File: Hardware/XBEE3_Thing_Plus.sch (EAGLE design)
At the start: 43 parts, among them Q1 2.5A/30V, U1 XBEE3_Micro, U2 MCP73831, U3 AP2112K-3.3V, U4 CP2102N

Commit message: v01 update
Removed test points from bottom of the board, removed the trace antenna, and modified the top ground pour as outlined in the XBee3 datasheet
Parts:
- removed E1: ANTENNA-GROUNDEDTRACE-15.2M_FLIPPED, SparkFun-RF:ANTENNA-GROUNDEDTRACE-15.2M_FLIPPED
- removed JP1: JUMPER-SMT_2_NC_TRACE_NO-SILK, SparkFun-Jumpers:JUMPER-SMT_2_NC_TRACE_NO-SILK
- added H1, H2: STAND-OFF, SparkFun-Hardware:STAND-OFF
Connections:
- removed net N$1: E1.SIGNAL, JP1.2
- removed net RF: JP1.1, U1.RF
- net GND: no longer E1.GND
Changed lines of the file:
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@@
 <part name="H3" library="SparkFun-Hardware" deviceset="STAND-OFF" device=""/>
 <part name="H4" library="SparkFun-Hardware" deviceset="STAND-OFF" device=""/>
-<part name="JP1" library="SparkFun-Jumpers" deviceset="JUMPER-SMT_2_NC_TRACE" device="_NO-SILK" value=""/>
 <part name="GND26" library="SparkFun-Aesthetics" deviceset="GND" device=""/>
 <part name="SUPPLY14" library="SparkFun-Aesthetics" deviceset="V_USB" device=""/>
@@
 <part name="FD3" library="SparkFun-Aesthetics" deviceset="FIDUCIAL" device="UFIDUCIAL" value="FIDUCIALUFIDUCIAL"/>
 <part name="FD4" library="SparkFun-Aesthetics" deviceset="FIDUCIAL" device="UFIDUCIAL" value="FIDUCIALUFIDUCIAL"/>
-<part name="E1" library="SparkFun-RF" deviceset="ANTENNA-GROUNDED" device="TRACE-15.2M_FLIPPED"/>
-<part name="GND18" library="SparkFun-PowerSymbols" deviceset="GND" device=""/>
 <part name="U$63" library="SparkFun-Aesthetics" deviceset="QWIIC_LOGO" device="_5MM" value="QWIIC_LOGO_5MM"/>
 <part name="J4" library="SparkFun-Connectors" deviceset="JST_2MM_MALE" device=""/>
 <part name="LOGO1" library="SparkFun-Aesthetics" deviceset="SFE_LOGO_NAME_FLAME" device=".1_INCH" value="SFE_LOGO_NAME_FLAME.1_INCH"/>
 <part name="LOGO2" library="SparkFun-Aesthetics" deviceset="OSHW-LOGO" device="S" value="OSHW-LOGOS"/>
+<part name="H1" library="SparkFun-Hardware" deviceset="STAND-OFF" device=""/>
+<part name="H2" library="SparkFun-Hardware" deviceset="STAND-OFF" device=""/>
 </parts>
 <sheets>
@@
 <instance part="H3" gate="G$1" x="241.3" y="33.02" smashed="yes"/>
 <instance part="H4" gate="G$1" x="241.3" y="30.48" smashed="yes"/>
-<instance part="JP1" gate="G$1" x="167.64" y="83.82" smashed="yes">
-<attribute name="NAME" x="165.1" y="86.36" size="1.778" layer="95" font="vector"/>
-<attribute name="VALUE" x="165.1" y="81.28" size="1.778" layer="96" font="vector" align="top-left"/>
-</instance>
 <instance part="GND26" gate="1" x="15.24" y="58.42" smashed="yes">
 <attribute name="VALUE" x="12.7" y="55.88" size="1.778" layer="96"/>
@@
 <instance part="FD3" gate="G$1" x="233.68" y="33.02" smashed="yes"/>
 <instance part="FD4" gate="G$1" x="233.68" y="30.48" smashed="yes"/>
-<instance part="E1" gate="G$1" x="175.26" y="96.52" smashed="yes">
-<attribute name="NAME" x="178.308" y="91.44" size="1.778" layer="95" font="vector"/>
-</instance>
-<instance part="GND18" gate="1" x="177.8" y="78.74" smashed="yes">
-<attribute name="VALUE" x="177.8" y="78.486" size="1.778" layer="96" align="top-center"/>
-</instance>
 <instance part="U$63" gate="G$1" x="137.16" y="5.08" smashed="yes"/>
 <instance part="J4" gate="G$1" x="167.64" y="160.02" smashed="yes" rot="MR90">
@@
 <instance part="LOGO1" gate="G$1" x="190.5" y="35.56" smashed="yes"/>
 <instance part="LOGO2" gate="G$1" x="113.538" y="11.176" smashed="yes"/>
+<instance part="H1" gate="G$1" x="243.84" y="30.48" smashed="yes"/>
+<instance part="H2" gate="G$1" x="243.84" y="33.02" smashed="yes"/>
 </instances>
 <busses>
@@
 <wire x1="228.6" y1="154.94" x2="233.68" y2="154.94" width="0.1524" layer="91"/>
 <label x="233.68" y="154.94" size="1.27" layer="95" rot="MR180" xref="yes"/>
-</segment>
-</net>
-<net name="RF" class="0">
-<segment>
-<pinref part="U1" gate="G$1" pin="RF"/>
-<pinref part="JP1" gate="G$1" pin="1"/>
-<wire x1="157.48" y1="83.82" x2="162.56" y2="83.82" width="0.1524" layer="91"/>
 </segment>
 </net>
@@
 <pinref part="GND17" gate="1" pin="GND"/>
 <wire x1="22.86" y1="15.24" x2="22.86" y2="12.7" width="0.1524" layer="91"/>
-</segment>
-<segment>
-<pinref part="E1" gate="G$1" pin="GND"/>
-<wire x1="177.8" y1="86.36" x2="177.8" y2="81.28" width="0.1524" layer="91"/>
-<pinref part="GND18" gate="1" pin="GND"/>
 </segment>
 <segment>
@@
 </segment>
 </net>
-<net name="N$1" class="0">
-<segment>
-<pinref part="JP1" gate="G$1" pin="2"/>
-<wire x1="175.26" y1="86.36" x2="175.26" y2="83.82" width="0.1524" layer="91"/>
-<wire x1="175.26" y1="83.82" x2="172.72" y2="83.82" width="0.1524" layer="91"/>
-<pinref part="E1" gate="G$1" pin="SIGNAL"/>
-</segment>
-</net>

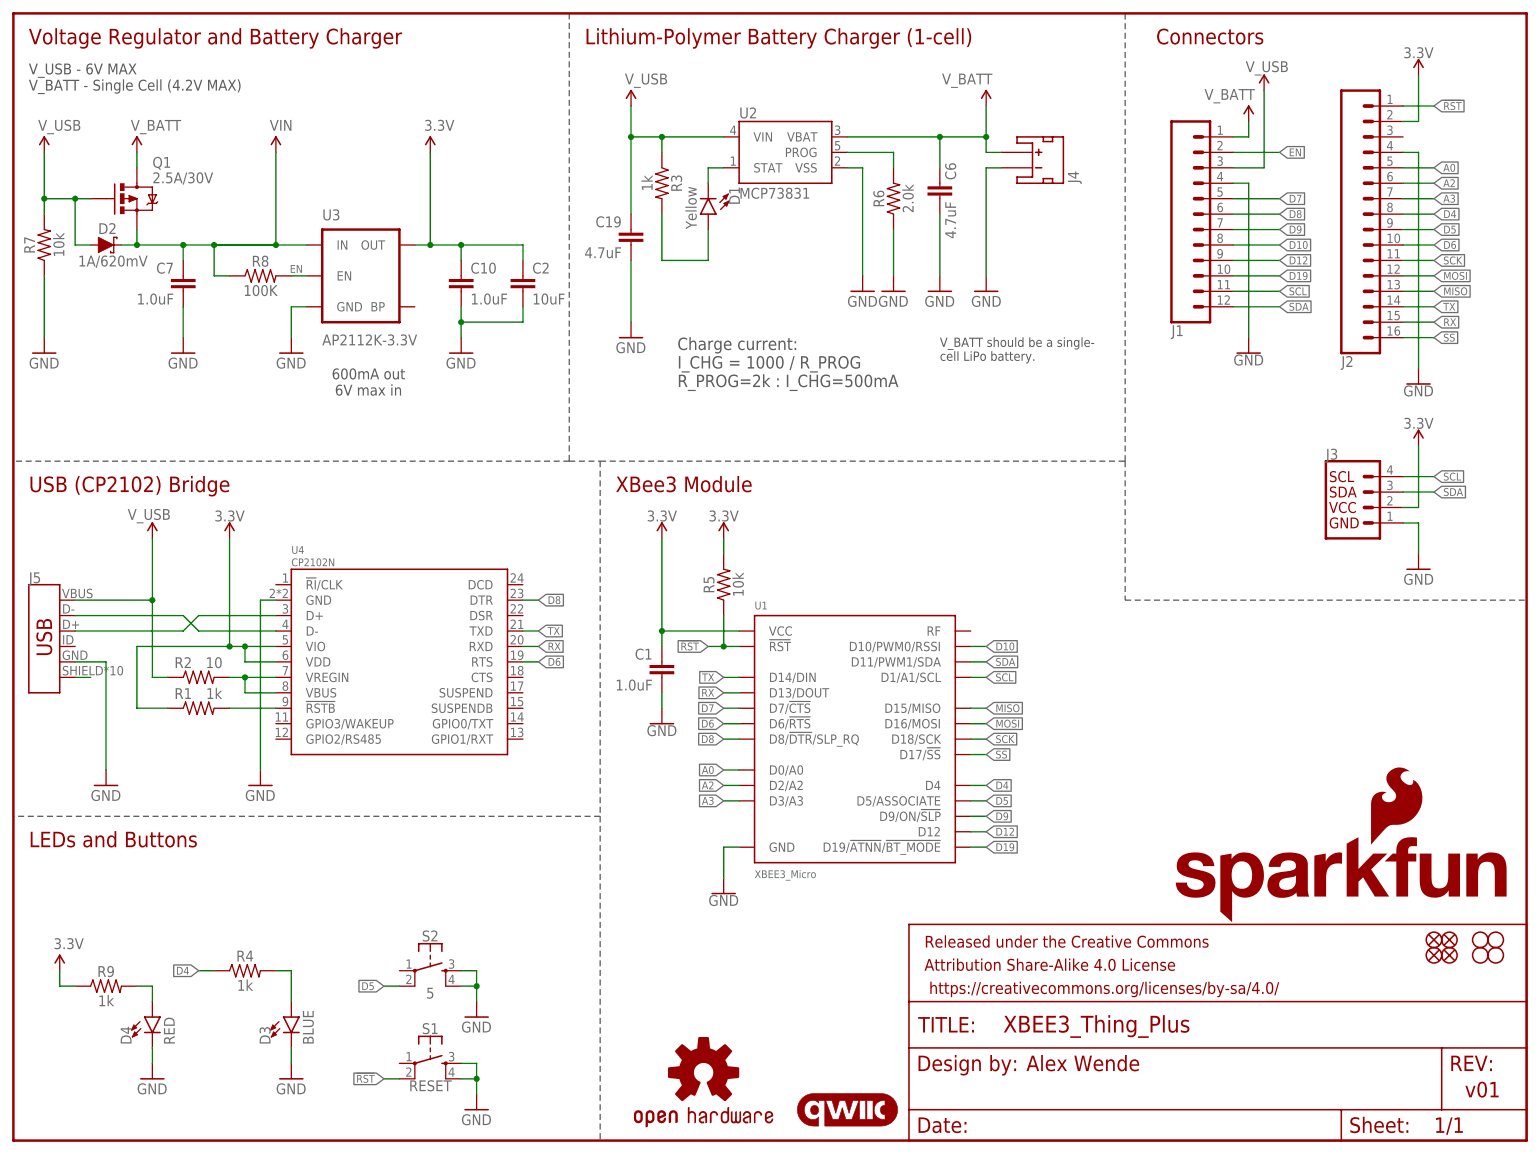
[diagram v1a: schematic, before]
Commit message: v01 Design Review Changes
- Adjusted R2
- Modified bottom ground pour
- Swapped D17 and extra ground header pads
- Updated buzzard labels
- Rotated name and logo on bottom
- Added SparkFun name logo to top of board
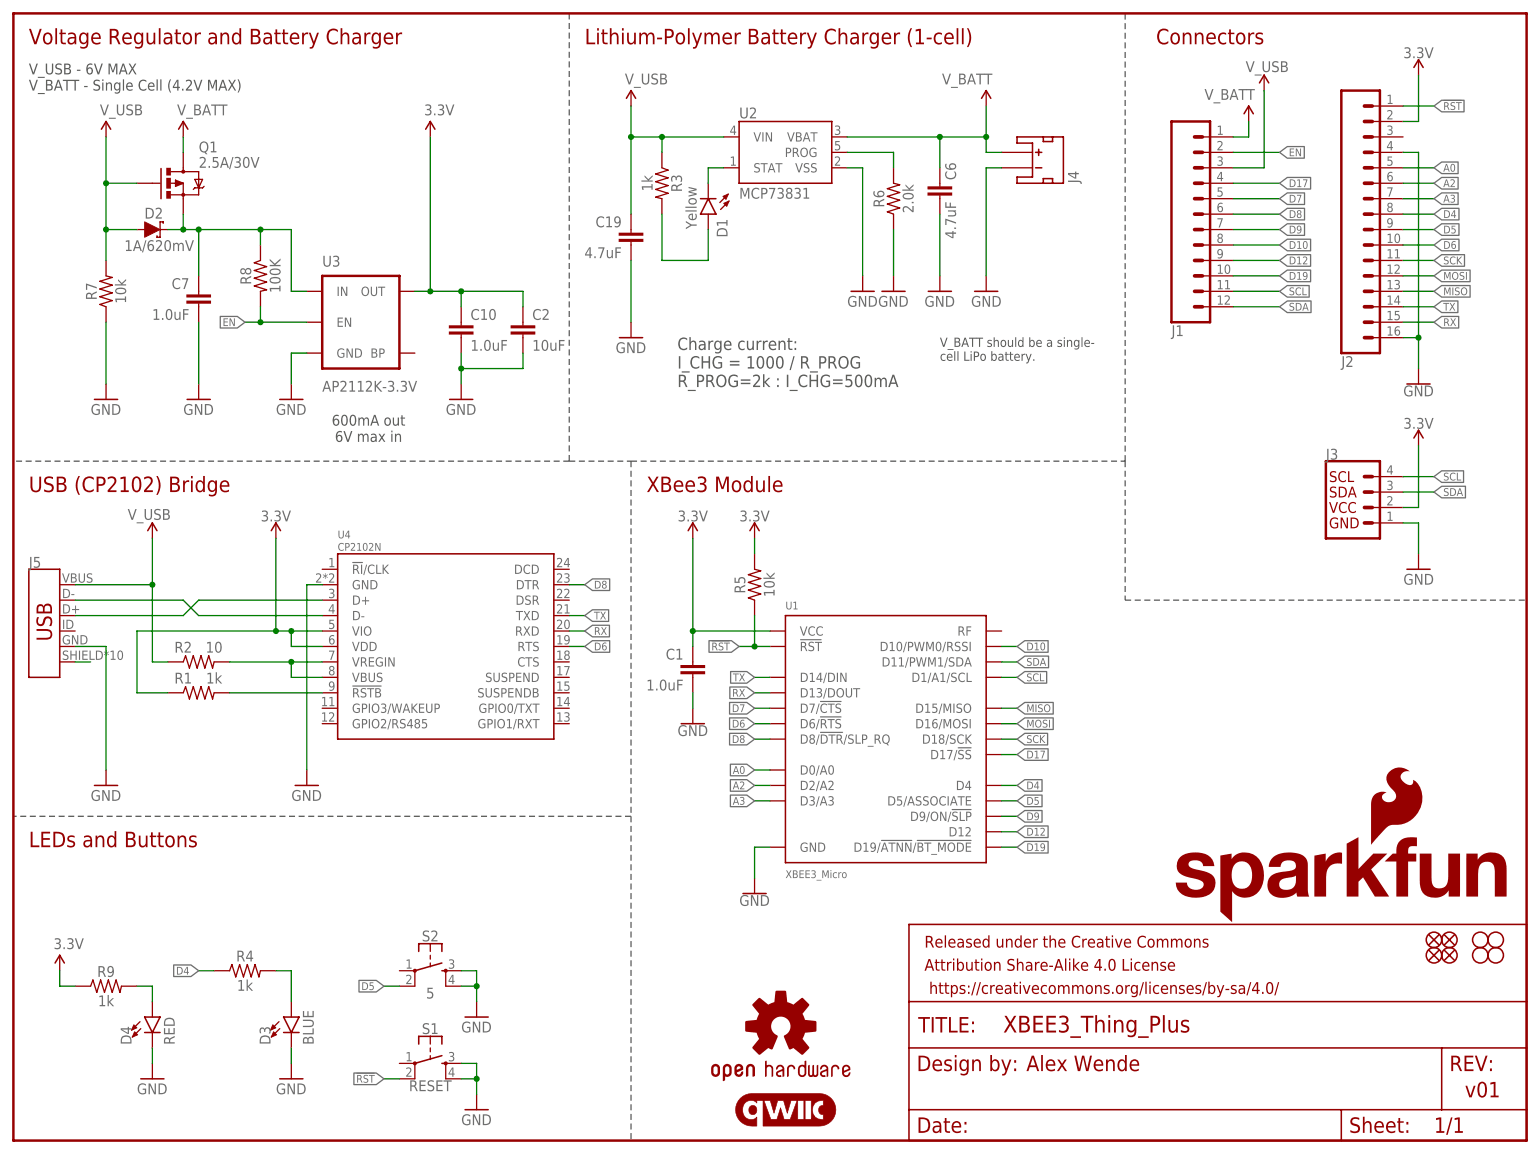
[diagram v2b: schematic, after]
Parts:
- C19, C6: device SparkFun-Capacitors:4.7UF0603 -> SparkFun-Capacitors:4.7UF-0603-6.3V-(10%)
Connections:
- net VIN renamed N$1
- removed net SS: J2.16, U1.D17/!SS
- new net D17: J1.4, U1.D17/!SS
- net GND: now also J2.16; no longer J1.4
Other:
- moved on the sheet: C1, C10, C2, C7, D2, J5, Q1, R1, R2, R5, R7, R8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

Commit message: v10
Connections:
- net RX renamed D13
- net SCL renamed D1
- net SDA renamed D11
- net TX renamed D14
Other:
- note added: "v10"
- note removed: "v01"
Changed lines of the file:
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@@
 <text x="93.98" y="180.34" size="2.54" layer="94" font="vector">Lithium-Polymer Battery Charger (1-cell)</text>
 <text x="166.624" y="11.43" size="2.54" layer="94" font="vector">Alex Wende</text>
-<text x="238.76" y="7.112" size="2.54" layer="94" font="vector">v01</text>
+<text x="238.76" y="7.112" size="2.54" layer="94" font="vector">v10</text>
 <wire x1="91.44" y1="185.42" x2="91.44" y2="111.76" width="0.1524" layer="97" style="shortdash"/>
 <wire x1="91.44" y1="111.76" x2="0" y2="111.76" width="0.1524" layer="97" style="shortdash"/>
@@
 </segment>
 </net>
-<net name="SDA" class="0">
+<net name="D11" class="0">
 <segment>
 <pinref part="U1" gate="G$1" pin="D11/PWM1/SDA"/>
@@
 </segment>
 </net>
-<net name="SCL" class="0">
+<net name="D1" class="0">
 <segment>
 <pinref part="U1" gate="G$1" pin="D1/A1/SCL"/>
@@
 </segment>
 </net>
-<net name="RX" class="0">
+<net name="D13" class="0">
 <segment>
 <pinref part="U4" gate="G$1" pin="RXD"/>
@@
 </segment>
 </net>
-<net name="TX" class="0">
+<net name="D14" class="0">
 <segment>
 <pinref part="U4" gate="G$1" pin="TXD"/>
@@
 </sheet>
 </sheets>
+<errors>
+</errors>
 </schematic>
 </drawing>

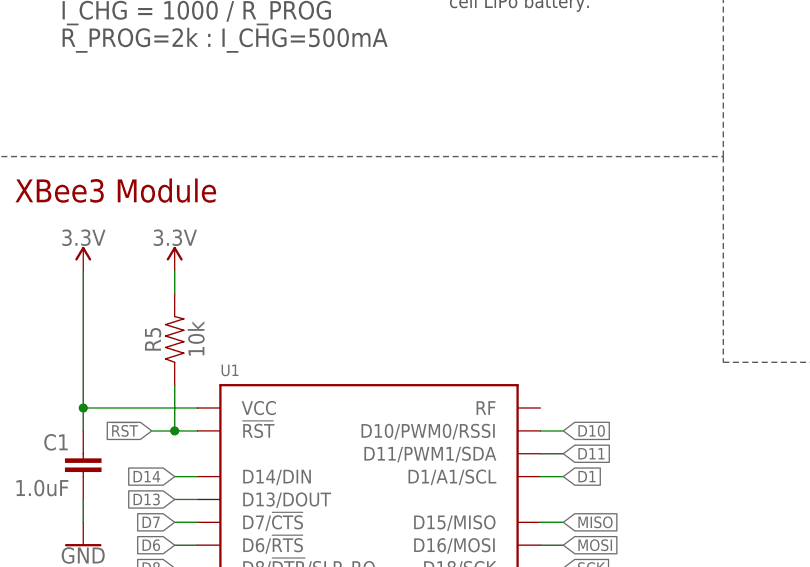
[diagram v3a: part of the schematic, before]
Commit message: v10 design review changes
Added input voltage range note for the XBee3 module in schematic
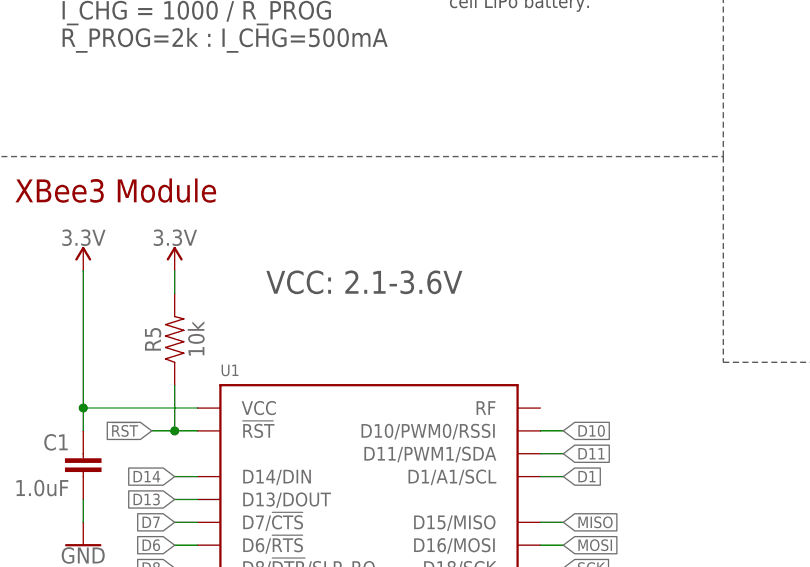
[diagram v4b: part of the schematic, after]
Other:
- note added: "VCC: 2.1-3.6V"
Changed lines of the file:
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@@
 <wire x1="182.88" y1="88.9" x2="248.92" y2="88.9" width="0.1524" layer="97" style="shortdash"/>
 <text x="2.54" y="48.26" size="2.54" layer="94" font="vector">LEDs and Buttons</text>
+<text x="132.08" y="96.52" size="2.54" layer="97" font="vector">VCC: 2.1-3.6V</text>
 </plain>
 <instances>
